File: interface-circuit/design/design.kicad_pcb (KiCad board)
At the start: 2 copper layers, 126.8 x 83.8 mm, 23 parts, among them J10 FAN_RELAY, J11 Conn_Switch, J12 Conn_Reset, J2 Screw_Term_RPi, J3 Screw_Term_Detector, J4 12V_IN, J5 Conn_Pwr_LED, J6 Conn_Piezo, J7 Conn_Printer_Mode, J8 Conn_Fan_Mode, J9 PRINTER_RELAY, Q1 2N3904-AP, Q2 2N3904-AP, Q3 2N3904-AP, U1 LogicLevelConverter_BOB-08745

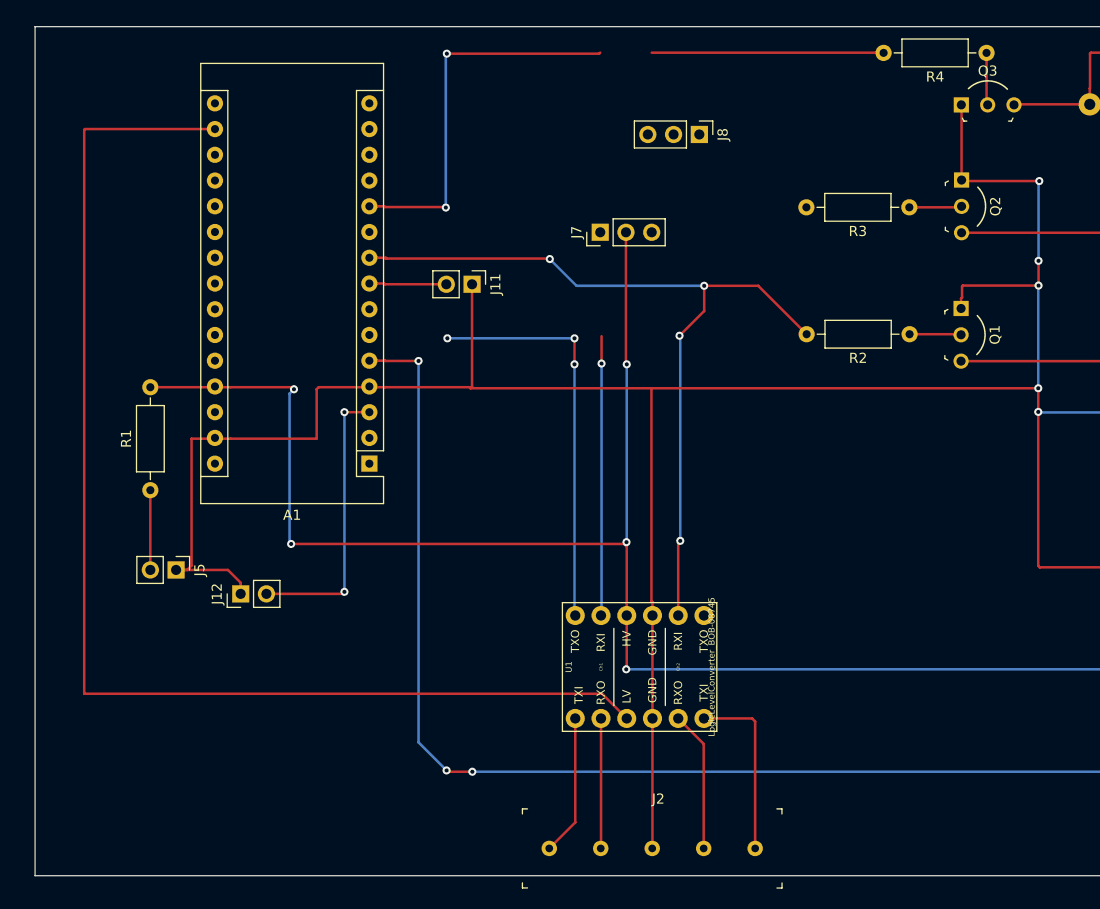
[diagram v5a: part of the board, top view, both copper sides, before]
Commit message: Changed protoboard layout so that we are using pins from both sides of the Arduino
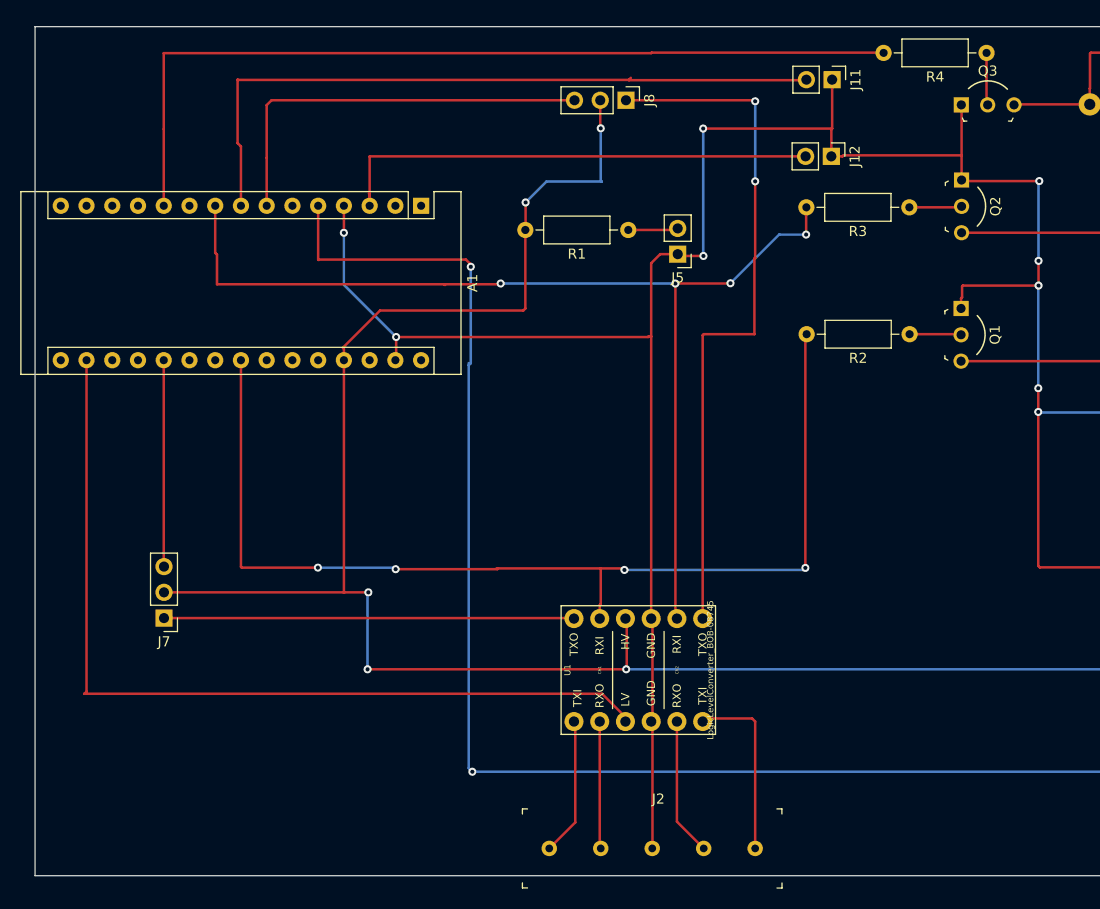
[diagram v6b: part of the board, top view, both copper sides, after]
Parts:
- moved J12 72.5 mm to (101.5, 89.0), turned to 270 degrees
- moved J5 58.5 mm to (86.3, 98.6), turned to 180 degrees
- moved J7 57.5 mm to (35.6, 134.5), turned to 180 degrees
- moved R1 53.7 mm to (81.5, 96.2), turned to 180 degrees
- moved J11 40.9 mm to (101.6, 81.4)
- moved A1 26.0 mm to (61.0, 93.9), turned to 270 degrees
- moved J8 7.99 mm to (81.2, 83.4)
- moved U1 0.33 mm to (82.4, 139.7)
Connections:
- A1 pad 1: Net-(A1-Pad1) -> (no net)
- A1 pad 10: /D7_PRINTER_RELAY -> (no net)
- A1 pad 12: Net-(A1-Pad12) -> (no net)
- A1 pad 13: Net-(A1-Pad13) -> (no net)
- A1 pad 14: Net-(A1-Pad14) -> (no net)
- A1 pad 15: Net-(A1-Pad15) -> (no net)
- A1 pad 16: Net-(A1-Pad16) -> (no net)
- A1 pad 18: Net-(A1-Pad18) -> (no net)
- A1 pad 19: Net-(A1-Pad19) -> (no net)
- A1 pad 2: Net-(A1-Pad2) -> (no net)
- A1 pad 20: Net-(A1-Pad20) -> /SW_PRINTER_RELAY
- A1 pad 21: Net-(A1-Pad21) -> (no net)
- A1 pad 22: Net-(A1-Pad22) -> (no net)
- A1 pad 23: Net-(A1-Pad23) -> /HV_AlarmTriggered
- A1 pad 24: Net-(A1-Pad24) -> (no net)
- A1 pad 25: Net-(A1-Pad25) -> (no net)
- A1 pad 26: Net-(A1-Pad26) -> (no net)
- A1 pad 28: Net-(A1-Pad28) -> (no net)
- A1 pad 30: Net-(A1-Pad30) -> (no net)
- A1 pad 6: /SW_PRINTER_RELAY -> (no net)
- A1 pad 9: /HV_AlarmTriggered -> /D7_PRINTER_RELAY
- J2 pad 2: /LV_PrinterPowerStatus -> /LV_AlarmTriggered
- J2 pad 4: /LV_AlarmTriggered -> /LV_PrinterPowerStatus
- J3 pad 4: Net-(J3-Pad4) -> (no net)
- U1 pad 1: /D7_PRINTER_RELAY -> /HV_AlarmTriggered
- U1 pad 10: /LV_AlarmTriggered -> /LV_PrinterPowerStatus
- U1 pad 2: /HV_AlarmTriggered -> /D7_PRINTER_RELAY
- U1 pad 9: /LV_PrinterPowerStatus -> /LV_AlarmTriggered
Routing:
- net /D7_PRINTER_RELAY: track 27.6 -> 104.0 mm, vias 1 -> 4
- net /HV_FanPowerDemand: track 0.00 -> 69.0 mm, vias 0 -> 2
- net /SOFT_SWITCH: track 7.63 -> 69.7 mm
- net /SW_FAN_RELAY: track 0.00 -> 40.5 mm
- net +3V3: track 123.1 -> 87.6 mm
- net /D8_FAN_RELAY: track 60.9 -> 86.1 mm, vias 2 -> 0
- net /HV_AlarmTriggered: track 80.1 -> 104.7 mm
- net +5V: track 176.3 -> 199.9 mm
- net /DETECTOR_SIGNAL: track 131.7 -> 153.9 mm, vias 4 -> 3
- net /RESET: track 28.1 -> 49.1 mm, vias 2 -> 0
- net /SW_PRINTER_RELAY: track 0.00 -> 20.4 mm
- net GND: track 285.1 -> 270.5 mm, vias 6 -> 10
- net Net-(J5-Pad2): track 7.87 -> 4.94 mm
- net /LV_AlarmTriggered: track 13.9 -> 12.6 mm
- net /LV_PrinterPowerStatus: track 12.8 -> 13.6 mm
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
